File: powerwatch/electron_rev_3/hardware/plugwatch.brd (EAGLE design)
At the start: 57.1 x 93 mm, 111 parts, among them J1 DM3AT-SF-PEJM5, J2 TC2030-JLINK-NL, U1 BGA725L6-ALT, U10 SIP32510, U11 SIP32510, U12 SIP32510, U13 SIP32510, U2 SAFFB1G56KB0F0A, U3 ISL29035, U4 MAX-M8, U5 MAX740XESA, U6 MPU-9250, U7 NRF51822QF, U8 OPA322AIDBVT, U9 SIP32510, X1 ABS05-32.768KHZ-9-T, X2 16MHz

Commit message: Tried to address a lot of #2
Still need prefilter audio output

Need a check over 60hz antenna stuff
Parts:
- added JP1: JUMPER-3SMD, SparkFun-Passives:SJ_3
- added L6: (no value), SparkFun-Passives:1X02
- added R26: 100k, passives:0402_RES
- added R27: 10k, passives:0402_RES
- added R28: 487k, passives:0402_RES
- added TP18, TP26: TEST_POINT_0.040IN, headers:TESTPOINT_0.040IN
- added U14: MPU-9250, chips:QFN-24/3MM
- added U15: OPA322AIDBVT, opamps:SOT23-5
- C27: device passives:0402_CAP -> passives:0805_CAP
- U6: value MPU-9250 -> SIP32510; device Testing:QFN24_PAD -> chips:TSOT23-6
- moved R11 6.68 mm to (9.65, 67.8)
- moved C19 5.80 mm to (8.13, 66.0), turned to 180 degrees
- moved U6 5.57 mm to (2.54, 73.9), turned to 180 degrees
- moved C18 4.85 mm to (9.65, 69.3), turned to 180 degrees
- moved C27 0.80 mm to (37.3, 40.1), turned to 0 degrees
- moved U11 0.51 mm to (19.3, 8.38)
- moved TP16 0.25 mm to (13.2, 52.6)
- moved R20 0.25 mm to (21.8, 8.64)
- moved R9 0.15 mm to (8.89, 73.7)
- moved R10 0.10 mm to (6.86, 73.7)
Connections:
- removed net REGOUT: C18.1, U6.10
- removed net SD_ENABLE_POWER: R17.1, U12.3
- new net 60HZ_AMP: ASSY1.B3, R28.2, U15.1
- new net 60HZ_TRACE: JP1.3
- new net INDUCTIVE_ANTENNA: JP1.1, L6.2
- new net N$19: C18.1, U14.10
- new net N$23: R27.2, R28.1, U15.4
- new net N$30: JP1.2, U15.3
- new net SD_ENABLE: ASSY1.D5, R17.1, U12.3
- new net SENSORS_PWR_EN: R26.1, U6.3
- new net VCC_SENSORS: C13.1, C17.1, C19.1, R10.2, R11.2, R8.2, R9.2, U14.1, U14.13, U14.22, U14.8, U3.1, U6.1, U6.2
- net !IMU_INT: now also U14.12; no longer U6.12
- net GND: now also C27.P$1, R27.1, TP26.TESTPOINT, U14.11, U14.18, U14.20, U14.9, U15.2, U6.4; no longer C27.1, U6.11, U6.18, U6.20, U6.9, U6.CENTER
- net GPS_VCC: now also C27.P$2; no longer C27.2
- net SENSORS_SCL: now also U14.23; no longer U6.23
- net SENSORS_SDA: now also U14.24; no longer U6.24
- net VCC: now also R26.2, TP18.TESTPOINT, U15.5, U6.5, U6.6; no longer C13.1, C17.1, C19.1, R10.2, R11.2, R8.2, R9.2, U3.1, U6.1, U6.13, U6.22, U6.8
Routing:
- net 60HZ_TRACE: track 0.00 -> 222.6 mm, vias 0 -> 2
- net VCC_SENSORS: track 0.00 -> 112.1 mm, vias 0 -> 8
- net SD_ENABLE: track 0.00 -> 27.7 mm, vias 0 -> 2
- net VCC: track 91.0 -> 70.4 mm, vias 10 -> 9
- net 60HZ_AMP: track 0.00 -> 19.1 mm
- net N$30: track 0.00 -> 11.8 mm
- net N$23: track 0.00 -> 5.44 mm
- net SD_ENABLE_POWER: track 4.97 -> 0.00 mm
- net SENSORS_SCL: track 70.5 -> 74.4 mm
- net !IMU_INT: track 33.5 -> 30.1 mm
- net INDUCTIVE_ANTENNA: track 0.00 -> 2.79 mm
- net SENSORS_SDA: track 99.4 -> 97.3 mm, vias 1 -> 3
- net REGOUT: track 1.91 -> 0.00 mm
- net SENSORS_PWR_EN: track 0.00 -> 1.41 mm
- net N$19: track 0.00 -> 1.39 mm
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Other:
- board text added: "AUDIO"
- board text added: "BLE"
- board text added: "BRD_ANT"
- board text added: "GND"
- board text added: "GPS"
- board text added: "IMU"
- board text added: "IND_ANT"
- board text added: "LIGHT"
- board text added: "SD CARD"
- board text added: "USB"
- board text added: "VCC"
- board text added: "WIFI"

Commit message: add plugwatch last fixes
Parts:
- added TP27, TP28: TEST_POINT_0.040IN, headers:TESTPOINT_0.040IN
- moved U$3 0.76 mm to (44.7, 79.5)
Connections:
- new net B0: ASSY1.B0, TP28.TESTPOINT
- net A_MIC_OUT: now also TP27.TESTPOINT
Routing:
- net A_MIC_OUT: track 7.92 -> 18.9 mm
- net B0: track 0.00 -> 3.82 mm
- net GND: vias 202 -> 201
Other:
- board text added: "B0"
- board text added: "MIC PRE-FILT"
- board text added: "NRF_SWDIO/ !RESET"
- board text removed: "NRF_SWDIO/!RESET"
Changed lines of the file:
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@@
 <setting verticaltext="up"/>
 </settings>
-<grid distance="10" unitdist="mil" unit="mil" style="lines" multiple="1" display="yes" altdistance="5" altunitdist="mil" altunit="mil"/>
+<grid distance="10" unitdist="mil" unit="mil" style="lines" multiple="1" display="yes" altdistance="10" altunitdist="mil" altunit="mil"/>
 <layers>
 <layer number="1" name="Top" color="4" fill="1" visible="yes" active="yes"/>
@@
 <text x="19.2532" y="54.6608" size="1.016" layer="48" font="vector" ratio="12" rot="R90" align="bottom-center">Cell Antenna below
 (No solid groundplane)</text>
-<text x="44.704" y="74.422" size="1.016" layer="25" font="vector" ratio="12">Noah Klugman
+<text x="44.704" y="73.66" size="1.016" layer="25" font="vector" ratio="12">Noah Klugman
 Branden Ghena
 Neal Jackson
 02/18</text>
-<text x="52.832" y="81.534" size="1.778" layer="25" font="vector" ratio="12">&gt;REV</text>
-<wire x1="52.578" y1="81.28" x2="54.356" y2="81.28" width="0.254" layer="25"/>
-<wire x1="54.356" y1="81.28" x2="54.356" y2="83.566" width="0.254" layer="25"/>
-<wire x1="54.356" y1="83.566" x2="52.578" y2="83.566" width="0.254" layer="25"/>
-<wire x1="52.578" y1="83.566" x2="52.578" y2="81.28" width="0.254" layer="25"/>
+<text x="52.832" y="80.264" size="1.778" layer="25" font="vector" ratio="12">&gt;REV</text>
+<wire x1="52.578" y1="80.01" x2="54.356" y2="80.01" width="0.254" layer="25"/>
+<wire x1="54.356" y1="80.01" x2="54.356" y2="82.296" width="0.254" layer="25"/>
+<wire x1="54.356" y1="82.296" x2="52.578" y2="82.296" width="0.254" layer="25"/>
+<wire x1="52.578" y1="82.296" x2="52.578" y2="80.01" width="0.254" layer="25"/>
 <text x="2.286" y="88.392" size="0.8128" layer="25" font="vector" ratio="12" rot="R90" align="bottom-center">WIFI_TXD</text>
 <text x="21.082" y="79.248" size="0.8128" layer="25" font="vector" ratio="12" rot="R270" align="bottom-center">WIFI_RXD</text>
@@
 <text x="20.32" y="38.354" size="0.8128" layer="25" font="vector" ratio="12" align="bottom-center">!SD_CS</text>
 <text x="23.622" y="35.052" size="0.8128" layer="25" font="vector" ratio="12" rot="R180" align="bottom-center">BLE_PWR_EN</text>
-<text x="24.384" y="30.734" size="0.8128" layer="25" font="vector" ratio="12" rot="R180" align="bottom-center">NRF_SWDIO/!RESET</text>
+<text x="22.86" y="30.734" size="0.8128" layer="25" font="vector" ratio="12" rot="R180" align="bottom-center">NRF_SWDIO/
+!RESET</text>
 <text x="17.526" y="52.832" size="0.8128" layer="25" font="vector" ratio="12" rot="R180" align="bottom-center">BLE_RXD</text>
 <text x="52.832" y="37.338" size="0.8128" layer="25" font="vector" ratio="12" rot="R90" align="bottom-center">AUDIO_PWR_EN</text>
@@
 <text x="51.562" y="68.326" size="0.8128" layer="25" font="vector" ratio="12" rot="R90" align="bottom-center">BRD_ANT</text>
 <text x="53.848" y="68.326" size="0.8128" layer="25" font="vector" ratio="12" rot="R90" align="bottom-center">IND_ANT</text>
+<wire x1="41.148" y1="30.988" x2="39.243" y2="30.988" width="0.127" layer="21" curve="-85.020894"/>
+<wire x1="39.243" y1="30.353" x2="41.148" y2="30.353" width="0.127" layer="21"/>
+<wire x1="43.561" y1="22.733" x2="45.466" y2="22.733" width="0.127" layer="21" curve="-85.020894"/>
+<wire x1="43.561" y1="23.368" x2="45.466" y2="23.368" width="0.127" layer="21"/>
+<wire x1="52.324" y1="25.781" x2="52.324" y2="27.686" width="0.127" layer="21" curve="-85.020894"/>
+<wire x1="51.562" y1="25.781" x2="51.562" y2="27.686" width="0.127" layer="21"/>
+<text x="28.956" y="30.734" size="0.8128" layer="25" font="vector" ratio="12" rot="R180" align="bottom-center">MIC
+PRE-FILT</text>
+<text x="48.006" y="85.598" size="0.8128" layer="25" font="vector" ratio="12" align="bottom-center">B0</text>
 </plain>
 <attributes>
@@
 <attribute name="VALUE" x="54.61" y="34.925" size="1.016" layer="27" font="vector" ratio="12" rot="R180" align="bottom-center"/>
 </element>
-<element name="U$3" library="logos" package="UCB_CAL_200MIL" value="" x="44.704" y="80.264" smashed="yes"/>
+<element name="U$3" library="logos" package="UCB_CAL_200MIL" value="" x="44.704" y="79.502" smashed="yes"/>
 <element name="TP1" library="headers" package="TESTPOINT_0.040IN" value="TEST_POINT_0.040IN" x="44.958" y="48.514" smashed="yes">
 <attribute name="DIGIKEY" value="5001K-ND" x="44.958" y="48.514" size="1.778" layer="27" display="off"/>
@@
 <attribute name="NAME" x="49.022" y="63.627" size="1.016" layer="25" font="vector" ratio="12" rot="R180" align="bottom-center"/>
 <attribute name="VALUE" x="49.022" y="65.405" size="1.016" layer="27" font="vector" ratio="12" rot="R180" align="bottom-center"/>
+</element>
+<element name="TP27" library="headers" package="TESTPOINT_0.040IN" value="TEST_POINT_0.040IN" x="27.94" y="32.258" smashed="yes">
+<attribute name="DIGIKEY" value="5001K-ND" x="27.94" y="32.258" size="1.778" layer="27" font="vector" ratio="12" display="off"/>
+<attribute name="VALUE" x="27.94" y="29.718" size="1.016" layer="27" font="vector" ratio="12" align="bottom-center"/>
+</element>
+<element name="TP28" library="headers" package="TESTPOINT_0.040IN" value="TEST_POINT_0.040IN" x="45.466" y="85.852" smashed="yes">
+<attribute name="DIGIKEY" value="5001K-ND" x="45.466" y="85.852" size="1.778" layer="27" font="vector" ratio="12" display="off"/>
+<attribute name="VALUE" x="45.466" y="83.312" size="1.016" layer="27" font="vector" ratio="12" align="bottom-center"/>
 </element>
 </elements>
@@
 <via x="49.53" y="21.59" extent="1-16" drill="0.3048"/>
 <via x="29.718" y="31.75" extent="1-16" drill="0.3048"/>
-<via x="28.702" y="34.544" extent="1-16" drill="0.3048"/>
-<via x="26.924" y="33.782" extent="1-16" drill="0.3048"/>
+<via x="28.702" y="34.798" extent="1-16" drill="0.3048"/>
 <via x="43.942" y="64.77" extent="1-16" drill="0.3048"/>
 <via x="44.704" y="64.008" extent="1-16" drill="0.3048"/>
@@
 <wire x1="44.3738" y1="34.925" x2="43.0814" y2="34.925" width="0.8128" layer="1"/>
 <wire x1="43.0814" y1="34.925" x2="40.0842" y2="31.9278" width="0.8128" layer="1"/>
+<contactref element="TP27" pad="TESTPOINT"/>
+<wire x1="37.7594" y1="31.9278" x2="37.7594" y2="32.5986" width="0.254" layer="1"/>
+<wire x1="37.7594" y1="32.5986" x2="37.338" y2="33.02" width="0.254" layer="1"/>
+<wire x1="37.338" y1="33.02" x2="28.702" y2="33.02" width="0.254" layer="1"/>
+<wire x1="28.702" y1="33.02" x2="27.94" y2="32.258" width="0.254" layer="1"/>
 </signal>
 <signal name="N$9">
@@
 <wire x1="22.098" y1="81.788" x2="12.8898125" y2="81.788" width="0.254" layer="16"/>
 <contactref element="TP12" pad="TESTPOINT"/>
-<wire x1="41.8338" y1="83.7692" x2="45.466" y2="87.4014" width="0.254" layer="16"/>
-<wire x1="45.466" y1="87.4014" x2="45.466" y2="88.9" width="0.254" layer="16"/>
-<wire x1="10.63590625" y1="84.04190625" x2="12.8898125" y2="81.788" width="0.254" layer="16"/>
+<wire x1="41.8338" y1="83.7692" x2="43.688" y2="85.598" width="0.254" layer="16"/>
+<wire x1="43.688" y1="85.598" x2="43.688" y2="87.884" width="0.254" layer="16"/>
+<wire x1="43.688" y1="87.884" x2="44.704" y2="88.9" width="0.254" layer="16"/>
+<wire x1="44.704" y1="88.9" x2="45.4406" y2="88.9" width="0.254" layer="16"/>
+<wire x1="45.4406" y1="88.9" x2="45.466" y2="88.9254" width="0.254" layer="16"/>
+<wire x1="45.466" y1="88.9254" x2="45.466" y2="88.9" width="0.254" layer="16"/>
+<wire x1="10.3498125" y1="84.328" x2="12.8898125" y2="81.788" width="0.254" layer="16"/>
 <wire x1="10.3498125" y1="84.328" x2="9.398" y2="85.2798125" width="0.254" layer="16"/>
 <wire x1="9.398" y1="85.2798125" x2="9.398" y2="86.106" width="0.254" layer="16"/>
@@
 <wire x1="5.334" y1="84.074" x2="5.588" y2="84.328" width="0.254" layer="16"/>
 <wire x1="5.588" y1="84.328" x2="10.3498125" y2="84.328" width="0.254" layer="16"/>
-<wire x1="10.3498125" y1="84.328" x2="10.63590625" y2="84.04190625" width="0.254" layer="16"/>
 <wire x1="5.69825" y1="83.20175" x2="6.67" y2="83.20175" width="0.254" layer="16"/>
 </signal>
@@
 <via x="20.828" y="24.384" extent="1-16" drill="0.3048"/>
 <wire x1="20.828" y1="24.384" x2="20.828" y2="25.654" width="0.254" layer="1"/>
-<wire x1="20.828" y1="25.654" x2="28.575" y2="33.401" width="0.254" layer="1"/>
-<wire x1="28.575" y1="33.401" x2="32.766" y2="37.592" width="0.254" layer="1"/>
+<wire x1="20.828" y1="25.654" x2="25.654" y2="30.48" width="0.254" layer="1"/>
+<wire x1="25.654" y1="30.48" x2="25.654" y2="33.528" width="0.254" layer="1"/>
+<wire x1="25.654" y1="33.528" x2="26.162" y2="34.036" width="0.254" layer="1"/>
+<wire x1="26.162" y1="34.036" x2="29.21" y2="34.036" width="0.254" layer="1"/>
 <wire x1="41.8338" y1="73.6092" x2="46.482" y2="68.961" width="0.254" layer="1"/>
 <wire x1="46.482" y1="68.961" x2="46.482" y2="40.894" width="0.254" layer="1"/>
@@
 <contactref element="TP9" pad="TESTPOINT"/>
 <wire x1="23.622" y1="36.576" x2="25.4" y2="36.576" width="0.254" layer="1"/>
-<wire x1="25.4" y1="36.576" x2="28.575" y2="33.401" width="0.254" layer="1"/>
 <contactref element="U11" pad="3"/>
 <wire x1="21.844" y1="9.06906875" x2="21.40481875" y2="9.50825" width="0.6096" layer="16"/>
@@
 <wire x1="20.828" y1="9.50825" x2="20.254" y2="9.50825" width="0.6096" layer="16"/>
 <wire x1="20.828" y1="24.384" x2="20.828" y2="9.50825" width="0.254" layer="16"/>
+<wire x1="32.766" y1="37.592" x2="29.21" y2="34.036" width="0.254" layer="1"/>
+<wire x1="25.4" y1="36.576" x2="25.654" y2="36.322" width="0.254" layer="1"/>
+<wire x1="25.654" y1="36.322" x2="25.654" y2="33.528" width="0.254" layer="1"/>
 </signal>
 <signal name="GND2">
@@
 <wire x1="29.464" y1="2.54" x2="56.134" y2="2.54" width="0.3048" layer="1"/>
 </signal>
+<signal name="B0">
+<contactref element="TP28" pad="TESTPOINT"/>
+<contactref element="ASSY1" pad="B0"/>
+<wire x1="41.8338" y1="86.3092" x2="45.0088" y2="86.3092" width="0.254" layer="1"/>
+<wire x1="45.0088" y1="86.3092" x2="45.466" y2="85.852" width="0.254" layer="1"/>
+</signal>
 </signals>
+<errors>
+</errors>
 </board>
 </drawing>

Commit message: add production files
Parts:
- D1, D2, D3: value LED0603 -> BLUE
- L6: value (none) -> 27uH
- S1: value B3U-1000P -> (none)
- X1: value ABS05-32.768KHZ-9-T -> 32.768k

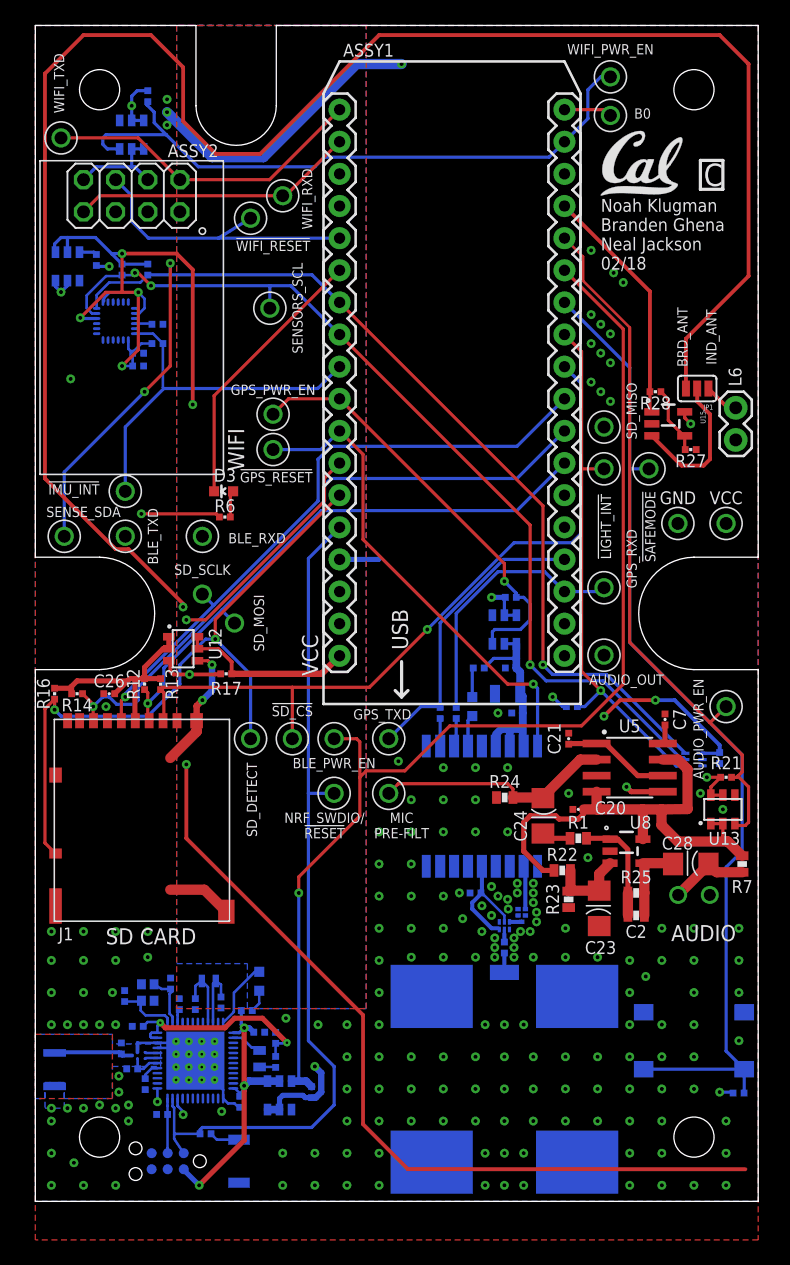
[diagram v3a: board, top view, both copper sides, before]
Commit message: added in dip switch, 1-wire serial number, removed rc filter
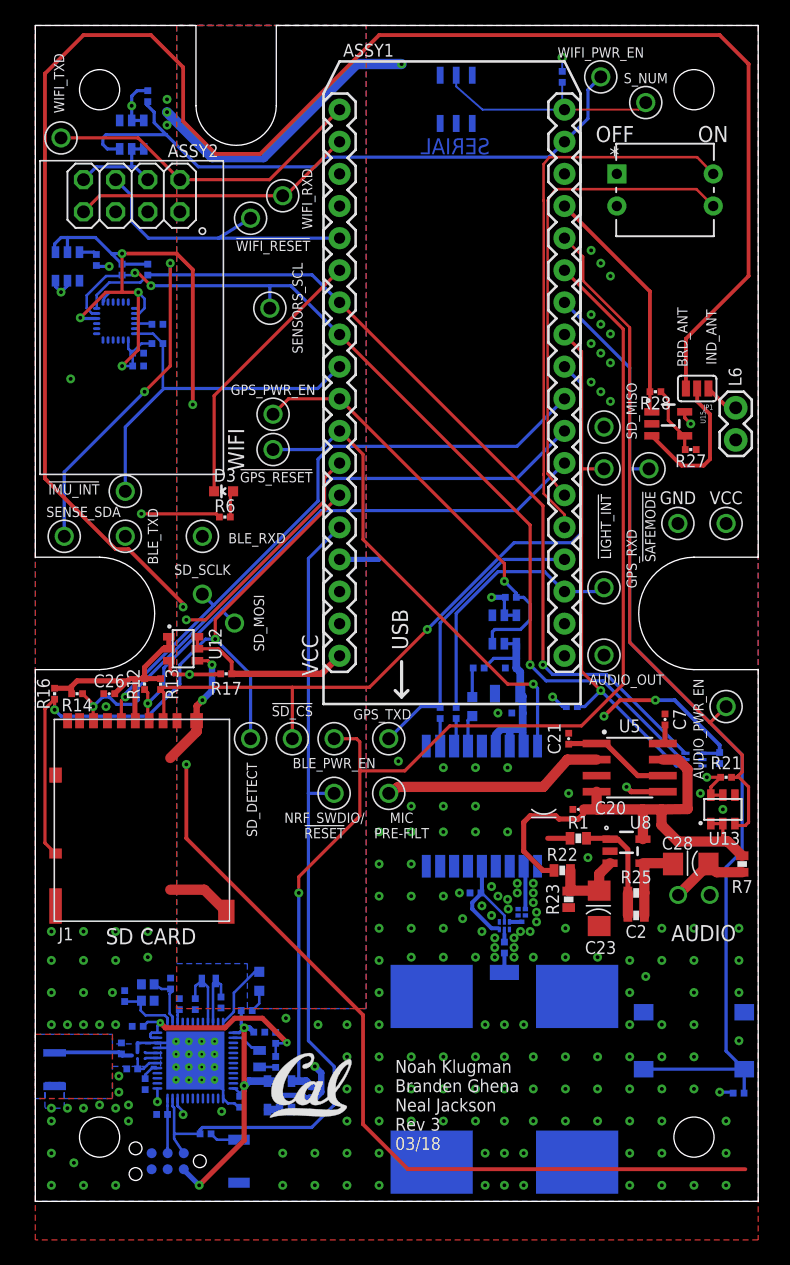
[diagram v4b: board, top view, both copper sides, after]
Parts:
- removed C24: 2.2uF, passives:1206
- removed R24: 100k, passives:0603-RES
- added R29: 5K, passives:0402_RES
- added SERIAL: DS2401P+, DS2401P+:21-0382
- added U16: 1825057-1, 18250571:SWDIP4_300X138P100
- moved U$3 77.5 mm to (18.5, 6.60)
- moved TP28 2.97 mm to (48.3, 86.9)
- moved TP12 0.76 mm to (44.7, 88.9)
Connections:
- removed net B0: ASSY1.B0, TP28.TESTPOINT
- new net APN_DIP_1: ASSY1.WKP, U16.4
- new net APN_DIP_2: ASSY1.DAC, U16.3
- new net SERIAL_NUM: ASSY1.B0, R29.2, SERIAL.2, TP28.TESTPOINT
- net A_MIC_OUT: no longer C24.1, R24.2
- net GND: now also SERIAL.1; no longer R24.1
- net N$7: no longer C24.2
- net VCC: now also R29.1, U16.1, U16.2
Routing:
- net APN_DIP_1: track 0.00 -> 43.6 mm
- net APN_DIP_2: track 0.00 -> 37.9 mm
- net SERIAL_NUM: track 0.00 -> 19.0 mm
- net B0: track 3.82 -> 0.00 mm
- net A_MIC_OUT: track 18.9 -> 17.6 mm
- net VCC: track 70.4 -> 71.5 mm, vias 9 -> 10
- net N$7: track 2.30 -> 1.77 mm
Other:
- board text added: "Noah Klugman Branden Ghena Neal Jackson Rev 3 03/18"
- board text added: "S_NUM"
- board text removed: ">REV"
- board text removed: "B0"
- board text removed: "Noah Klugman Branden Ghena Neal Jackson 02/18"

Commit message: apn labels
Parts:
- renumbered U16 to APN_SWITCH
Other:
- board text added: "(on, on)"
- board text added: "APN"
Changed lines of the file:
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@@
 <text x="8.89" y="52.578" size="0.8128" layer="25" font="vector" ratio="12" rot="R270" align="bottom-center">BLE_TXD</text>
 <text x="9.144" y="20.32" size="1.27" layer="25" font="vector" ratio="12" align="bottom-center">SD CARD</text>
+<text x="47.498" y="73.914" size="1.778" layer="25" font="vector" ratio="12">APN</text>
+<text x="47.752" y="72.644" size="0.8128" layer="25" font="vector" ratio="12">(on, on)</text>
 </plain>
 <attributes>
@@
 <attribute name="VALUE" x="43.053" y="88.9" size="1.016" layer="28" font="vector" ratio="12" rot="MR270" align="bottom-center"/>
 </element>
-<element name="U16" library="18250571" package="SWDIP4_300X138P100" value="1825057-1" x="53.594" y="78.6892" smashed="yes">
+<element name="APN_SWITCH" library="18250571" package="SWDIP4_300X138P100" value="1825057-1" x="53.594" y="78.6892" smashed="yes">
 <attribute name="MANUFACTURER_PART_NUMBER" value="18250571" x="53.594" y="78.6892" size="1.778" layer="27" display="off"/>
 <attribute name="VENDOR" value="TE Connectivity" x="53.594" y="78.6892" size="1.778" layer="27" display="off"/>
@@
 <via x="8.382" y="54.356" extent="1-16" drill="0.3048"/>
 <contactref element="R29" pad="1"/>
-<contactref element="U16" pad="1"/>
-<contactref element="U16" pad="2"/>
+<contactref element="APN_SWITCH" pad="1"/>
+<contactref element="APN_SWITCH" pad="2"/>
 <wire x1="41.656" y1="89.33306875" x2="41.656" y2="90.424" width="0.1524" layer="16"/>
 <via x="41.656" y="90.424" extent="1-16" drill="0.35"/>
@@
 <signal name="APN_DIP_1">
 <contactref element="ASSY1" pad="WKP"/>
-<contactref element="U16" pad="4"/>
+<contactref element="APN_SWITCH" pad="4"/>
 <wire x1="40.1955" y1="57.4097125" x2="40.182903125" y2="57.42564375" width="0.2032" layer="1"/>
 <wire x1="40.182903125" y1="57.42564375" x2="40.1955" y2="57.53343125" width="0.2032" layer="1"/>
@@
 <signal name="APN_DIP_2">
 <contactref element="ASSY1" pad="DAC"/>
-<contactref element="U16" pad="3"/>
+<contactref element="APN_SWITCH" pad="3"/>
 <wire x1="40.5003" y1="79.13634375" x2="41.13265625" y2="80.0227" width="0.2032" layer="1"/>
 <wire x1="40.5003" y1="57.51565625" x2="40.5003" y2="79.13634375" width="0.2032" layer="1"/>
